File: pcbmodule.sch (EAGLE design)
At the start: 13 parts, among them X11 MKDSN1,5/6-5,08, X5 MKDSN1,5/6-5,08, X8 MKDSN1,5/10-5,08, X9 MKDSN1,5/10-5,08

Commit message: add led indicator (bipolar red/green led: http://www.ledsales.com.au/index.php?main_page=product_info&products_id=1683)
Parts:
- added LED4, LED5, LED6: (no value), SparkFun-LED:LED5MM
- added R1, R2, R3: 2.5k, resistor:R-EU_0204/7
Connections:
- new net N$15: LED5.C, R1.2
- new net N$16: LED6.C, R2.2
- new net N$5: LED4.C, R3.2
- net N$1: now also R3.1
- net N$14: now also LED6.A
- net N$17: now also R2.1
- net N$2: now also LED4.A
- net N$4: now also R1.1
- net N$6: now also LED5.A
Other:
- moved on the sheet: X5-1, X5-3, X5-5

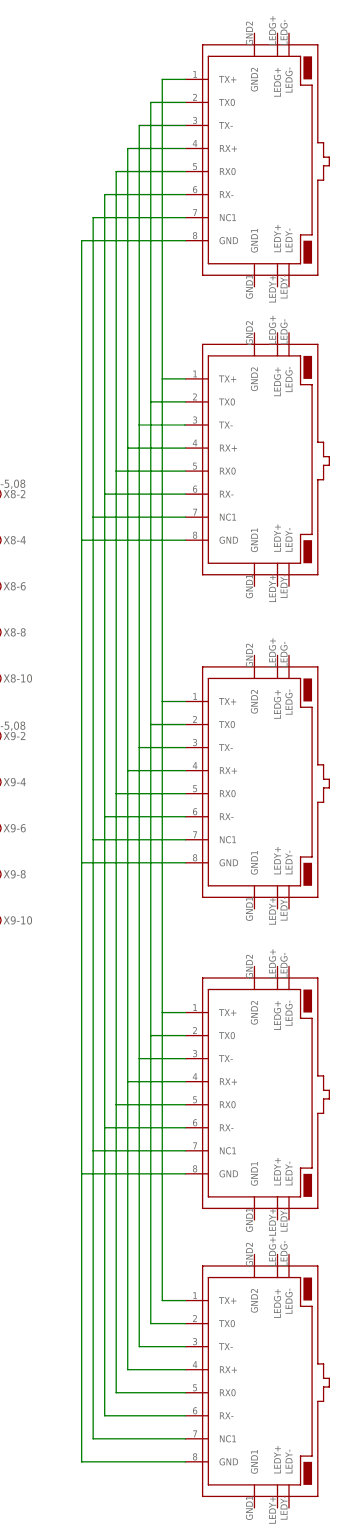
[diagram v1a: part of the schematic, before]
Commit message: update schema for proper RJ45 module layout
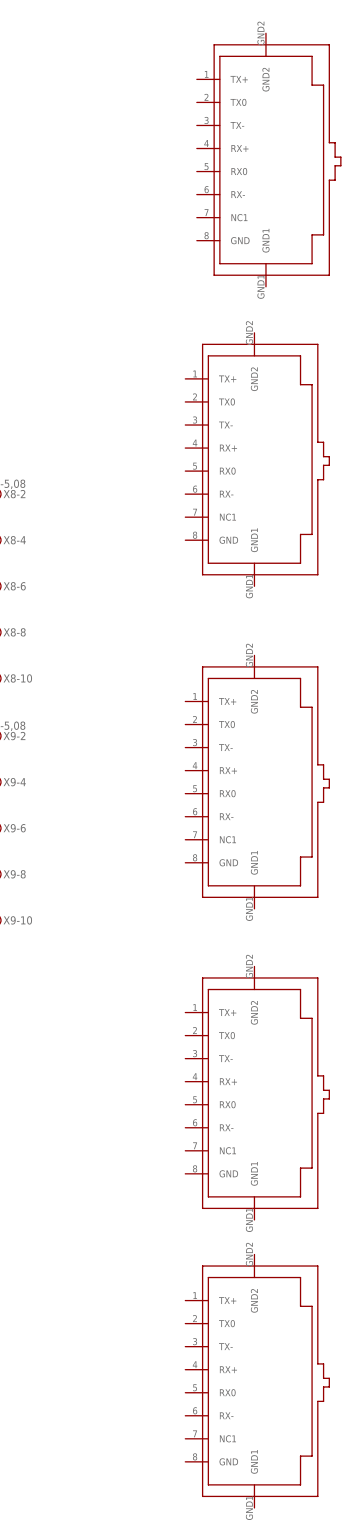
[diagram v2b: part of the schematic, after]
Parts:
- removed U$6: RJ45-TRAFO-L, con-amphenol-rj45-ld:RJ45-TRAFO-L
- added U$4: RJ45-TRAFO, con-amphenol-rj45-nzin:RJ45-TRAFO
- U$1, U$2, U$3, U$5: value RJ45-TRAFO-L -> RJ45-TRAFO; device con-amphenol-rj45-ld:RJ45-TRAFO-L -> con-amphenol-rj45-nzin:RJ45-TRAFO
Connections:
- removed net N$10: U$1.RX0, U$2.RX0, U$3.RX0, U$5.RX0, U$6.RX0
- removed net N$11: U$1.RX-, U$2.RX-, U$3.RX-, U$5.RX-, U$6.RX-
- removed net N$12: U$1.NC1, U$2.NC1, U$3.NC1, U$5.NC1, U$6.NC1
- removed net N$13: U$1.GND, U$2.GND, U$3.GND, U$5.GND, U$6.GND
- removed net N$3: U$1.TX+, U$2.TX+, U$3.TX+, U$5.TX+, U$6.TX+
- removed net N$7: U$1.TX0, U$2.TX0, U$3.TX0, U$5.TX0, U$6.TX0
- removed net N$8: U$1.TX-, U$2.TX-, U$3.TX-, U$5.TX-, U$6.TX-
- removed net N$9: U$1.RX+, U$2.RX+, U$3.RX+, U$5.RX+, U$6.RX+

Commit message: - change spec for rj12 (instead of rj45) - add a 4th circuit line for (analogic) metric n lines
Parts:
- added X6: MKDSN1,5/2-5,08, con-phoenix-508:MKDSN1,5/2-5,08
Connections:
- net N$18: now also X6-2.KL
- net N$19: now also X6-1.KL
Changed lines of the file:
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@@
 <part name="U$4" library="con-amphenol-rj45-nzin" deviceset="RJ45-TRAFO" device=""/>
 <part name="U$5" library="con-amphenol-rj45-nzin" deviceset="RJ45-TRAFO" device=""/>
+<part name="X6" library="con-phoenix-508" deviceset="MKDSN1,5/2-5,08" device=""/>
 </parts>
 <sheets>
@@
 <instance part="U$4" gate="G$1" x="121.92" y="-63.5"/>
 <instance part="U$5" gate="G$1" x="121.92" y="-127"/>
+<instance part="X6" gate="-1" x="48.26" y="-83.82"/>
+<instance part="X6" gate="-2" x="48.26" y="-91.44"/>
 </instances>
 <busses>
@@
 <pinref part="X4" gate="G$1" pin="7"/>
 <wire x1="33.02" y1="-22.86" x2="27.94" y2="-22.86" width="0.1524" layer="91"/>
+<wire x1="33.02" y1="-22.86" x2="33.02" y2="-91.44" width="0.1524" layer="91"/>
+<pinref part="X6" gate="-2" pin="KL"/>
+<wire x1="33.02" y1="-91.44" x2="45.72" y2="-91.44" width="0.1524" layer="91"/>
 </segment>
 </net>
@@
 <pinref part="X1" gate="G$1" pin="8"/>
 <wire x1="35.56" y1="53.34" x2="27.94" y2="53.34" width="0.1524" layer="91"/>
-</segment>
-</net>
+<wire x1="35.56" y1="-25.4" x2="35.56" y2="-83.82" width="0.1524" layer="91"/>
+<pinref part="X6" gate="-1" pin="KL"/>
+<wire x1="35.56" y1="-83.82" x2="45.72" y2="-83.82" width="0.1524" layer="91"/>
+</segment>
+</net>
